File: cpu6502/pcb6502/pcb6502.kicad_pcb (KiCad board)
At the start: 2 copper layers, 134.6 x 95.5 mm, 46 parts, among them J1 Power, J2 RS232, SW1 Reset, SW2 IRQ, SW3 Debug, U1 6502 (CPU), U2 28C256 (ROM), U3 62256 (RAM), U4 6522 (VIA), U5 74HC00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

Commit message: check point again
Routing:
- net /PHI2: track 242.6 -> 239.5 mm, vias 2 -> 1
- net /A11: track 114.5 -> 112.6 mm
- net /CS2: track 143.1 -> 144.2 mm
- net /D2: track 144.2 -> 145.2 mm
- net /R/W: track 188.4 -> 187.6 mm
- net /D1: track 137.6 -> 138.2 mm

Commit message: everything is working well!  OS still wip but pretty good
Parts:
- added J3: VIA PB, Connector_PinHeader_2.54mm:PinHeader_2x05_P2.54mm_Vertical, F.Cu at (76.2, 50.8)
- added J4: Reset Ext, Connector_PinHeader_2.54mm:PinHeader_1x02_P2.54mm_Vertical, F.Cu at (104.1, 29.2)
- C2, C3, C4, C5, C6: footprint Capacitor_THT:C_Disc_D3.0mm_W1.6mm_P2.50mm -> Capacitor_THT:C_Disc_D5.0mm_W2.5mm_P5.00mm
- R5: footprint Resistor_THT:R_Axial_DIN0204_L3.6mm_D1.6mm_P7.62mm_Horizontal -> Resistor_THT:R_Axial_DIN0204_L3.6mm_D1.6mm_P2.54mm_Vertical
- moved R5 8.03 mm to (99.1, 29.2), turned to -90 degrees
- moved SW2 5.09 mm to (76.2, 36.8)
- moved C6 2.58 mm to (191.8, 104.1)
- moved C2 2.50 mm to (191.8, 88.9)
- moved H3 1.42 mm to (74.9, 114.3)
- moved H2 1.27 mm to (74.9, 29.2)
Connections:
- U4 pad 10: unconnected-(U4-PB0-Pad10) -> /PB0
- U4 pad 11: unconnected-(U4-PB1-Pad11) -> /PB1
- U4 pad 12: unconnected-(U4-PB2-Pad12) -> /PB2
- U4 pad 13: unconnected-(U4-PB3-Pad13) -> /PB3
- U4 pad 14: unconnected-(U4-PB4-Pad14) -> /PB4
- U4 pad 15: unconnected-(U4-PB5-Pad15) -> /PB5
- U4 pad 16: unconnected-(U4-PB6-Pad16) -> /PB6
- U4 pad 17: unconnected-(U4-PB7-Pad17) -> /PB7
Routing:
- net +5V: track 500.4 -> 407.6 mm
- net /PB0: track 0.00 -> 87.0 mm
- net /PB1: track 0.00 -> 75.6 mm
- net /PB3: track 0.00 -> 72.6 mm
- net /PB2: track 0.00 -> 71.9 mm
- net /PB5: track 0.00 -> 67.7 mm
- net /PB4: track 0.00 -> 67.1 mm
- net /PB7: track 0.00 -> 62.0 mm
- net /PB6: track 0.00 -> 61.6 mm
- net GND: track 19.6 -> 0.00 mm, vias 1 -> 0
- net /RST: track 291.3 -> 305.4 mm
- net /VIAIRQ: track 58.4 -> 66.1 mm
- net /CA1: track 141.5 -> 148.7 mm, vias 1 -> 0
- net /ACIAIRQ: track 143.9 -> 150.5 mm
- net /R/W: track 187.6 -> 191.3 mm, vias 2 -> 3
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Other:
- board size 134.6 x 95.5 mm -> 135.9 x 95.3 mm
- board text added: "0"
- board text added: "0x0000 - 0x3FFF = RAM (16K) 0x4000 - 0x7FFF = I/O 0x8000 - 0xFFFF = ROM (32K)"
- board text added: "1"
- board text added: "2"
- board text added: "3"
- board text added: "4"
- board text added: "5"
- board text added: "5v"
- board text added: "6"
- board text added: "6502 OAComputer Rev 1.0"
- board text added: "7"
- board text added: "PCB Designed in 2023 by Chris Gall"
- board text added: "Thanks Ben Eater for the inspiration! https://eater.net/6502"
- board text removed: "0x0000 - 0x004F = Reserved OS RAM 0x0050 - 0x00FF = User Zero Page RAM 0x0100 - 0x01FF = Reserved Stack RAM 0x0300 - 0x3FFF = User Program/RAM (~15K) 0x4000 - 0x7FFF = Reserved Hardware 0x8000 - 0xFFFF = ROM (32K)"
- board text removed: "6502 Computer Rev v1.0"

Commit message: check point
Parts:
- removed D10: 4, LED_THT:LED_D3.0mm
- removed D11: 5, LED_THT:LED_D3.0mm
- removed D12: 6, LED_THT:LED_D3.0mm
- removed D13: 7, LED_THT:LED_D3.0mm
- removed D5: 0, LED_THT:LED_D3.0mm
- removed D6: 1, LED_THT:LED_D3.0mm
- removed D8: 2, LED_THT:LED_D3.0mm
- removed D9: 3, LED_THT:LED_D3.0mm
- removed RN2: 220, Resistor_THT:R_Array_SIP8
- C2, C3, C4, C5: value 1uf -> 1µF
- C6: value 20pf -> 20pF
- C7: value 1uF -> 1µF
- C8: value 0.1uf -> 0.1µF
- J3: value VIA PB -> VIA; footprint Connector_PinHeader_2.54mm:PinHeader_2x05_P2.54mm_Vertical -> Connector_PinHeader_2.54mm:PinHeader_2x09_P2.54mm_Vertical
- R3: value 1K -> 1KΩ
- R4: value 1M -> 1MΩ
- R5: value 1K -> 1KΩ; footprint Resistor_THT:R_Axial_DIN0204_L3.6mm_D1.6mm_P2.54mm_Vertical -> Resistor_THT:R_Axial_DIN0204_L3.6mm_D1.6mm_P7.62mm_Horizontal
- RN1: value 220 -> Resistor Array 220Ω (3); footprint Resistor_THT:R_Array_SIP8 -> Resistor_THT:R_Array_SIP6
- SW2: value IRQ -> Interrupts; footprint Button_Switch_THT:SW_DIP_SPSTx03_Slide_9.78x9.8mm_W7.62mm_P2.54mm -> Button_Switch_THT:SW_DIP_SPSTx06_Slide_9.78x17.42mm_W7.62mm_P2.54mm
- moved J3 70.4 mm to (115.6, 109.2), turned to -90 degrees
- moved RN1 30.5 mm to (148.6, 109.2), turned to 180 degrees
- moved R5 5.08 mm to (99.1, 34.3), turned to 90 degrees
- moved SW2 0.26 mm to (76.2, 36.6)
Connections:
- J3 pad 1: /PB0 -> /PA0
- J3 pad 10: GND -> /PB3
- J3 pad 2: /PB1 -> /PB7
- J3 pad 3: /PB2 -> /PA1
- J3 pad 4: /PB3 -> /PB6
- J3 pad 5: /PB4 -> /PA2
- J3 pad 7: /PB6 -> /PA3
- J3 pad 8: /PB7 -> /PB4
- J3 pad 9: +5V -> /PA4
- RN1 pad 2: /RNPA6 -> /RNPA0
- RN1 pad 3: /RNPA5 -> GND
- RN1 pad 4: /RNPA4 -> /RNPA1
- RN1 pad 5: /RNPA3 -> GND
- SW2 pad 4: /VIAIRQ -> /NMI
- SW2 pad 5: /ACIAIRQ -> /NMI
- SW2 pad 6: +5V -> /NMI
- U1 pad 6: +5V -> /NMI
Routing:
- net /NMI: track 0.00 -> 50.0 mm
- net +5V: track 407.6 -> 445.5 mm
- net /PB7: track 62.0 -> 80.1 mm
- net /PB0: track 87.0 -> 69.7 mm
- net /PB6: track 61.6 -> 78.8 mm
- net /PA0: track 59.5 -> 43.6 mm
- net /PA7: track 80.3 -> 69.3 mm
- net /PA1: track 57.4 -> 46.5 mm
- net /RNPA6: track 10.5 -> 0.00 mm
- net /PB5: track 67.7 -> 77.3 mm
- net /RNPA0: track 15.3 -> 6.13 mm
- net /RNPA5: track 8.54 -> 0.00 mm
- net /PA6: track 73.9 -> 65.3 mm
- net /PB4: track 67.1 -> 75.6 mm
- net /RNPA10: track 8.02 -> 0.00 mm
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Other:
- board text added: ". . . . . . ."
- board text added: "ACIA: 5000 - DATA 5001 - STATUS 5002 - COMMAND 5003 - CONTROL"
- board text added: "IRQ"
- board text added: "MEMORY MAP: 0000-3FFF RAM 4000-4FFF N/A 5000-5FFF ACIA 6000-6FFF VIA 7000-7FFF N/A 8000-FFFF ROM"
- board text added: "NMI"
- board text added: "PA0"
- board text added: "PA7"
- board text added: "PB0"
- board text added: "PB7"
- board text added: "VIA: CA1 - DEBUG PB/A - 6000/1 DDRB/A - 6002/3 A/PCR - 600B/C IF/IER - 600D/E"
- board text removed: "0"
- board text removed: "0x0000 - 0x3FFF = RAM (16K) 0x4000 - 0x7FFF = I/O 0x8000 - 0xFFFF = ROM (32K)"
- board text removed: "1"
- board text removed: "2"
- board text removed: "3"
- board text removed: "4"
- board text removed: "5"
- board text removed: "5v"
- board text removed: "6"
- board text removed: "7"
- board text removed: "Gnd"
- board text removed: "RS232, 19200 Baud 8 data bits 1 Stop Bit, No Parity CR only, UPPER case VT100 Emulation"
- board text removed: "User/Status"

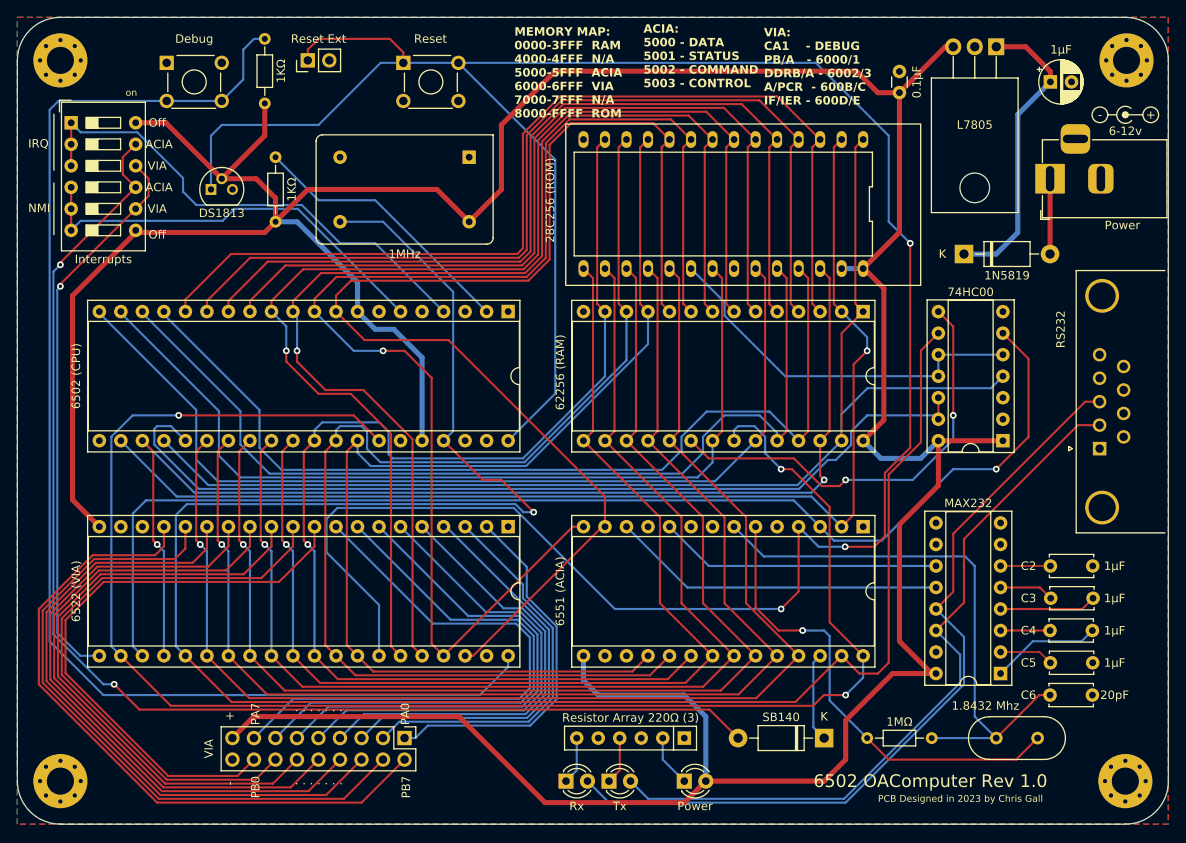
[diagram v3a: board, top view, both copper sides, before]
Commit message: rs232 nmi / cts, circuit close to done
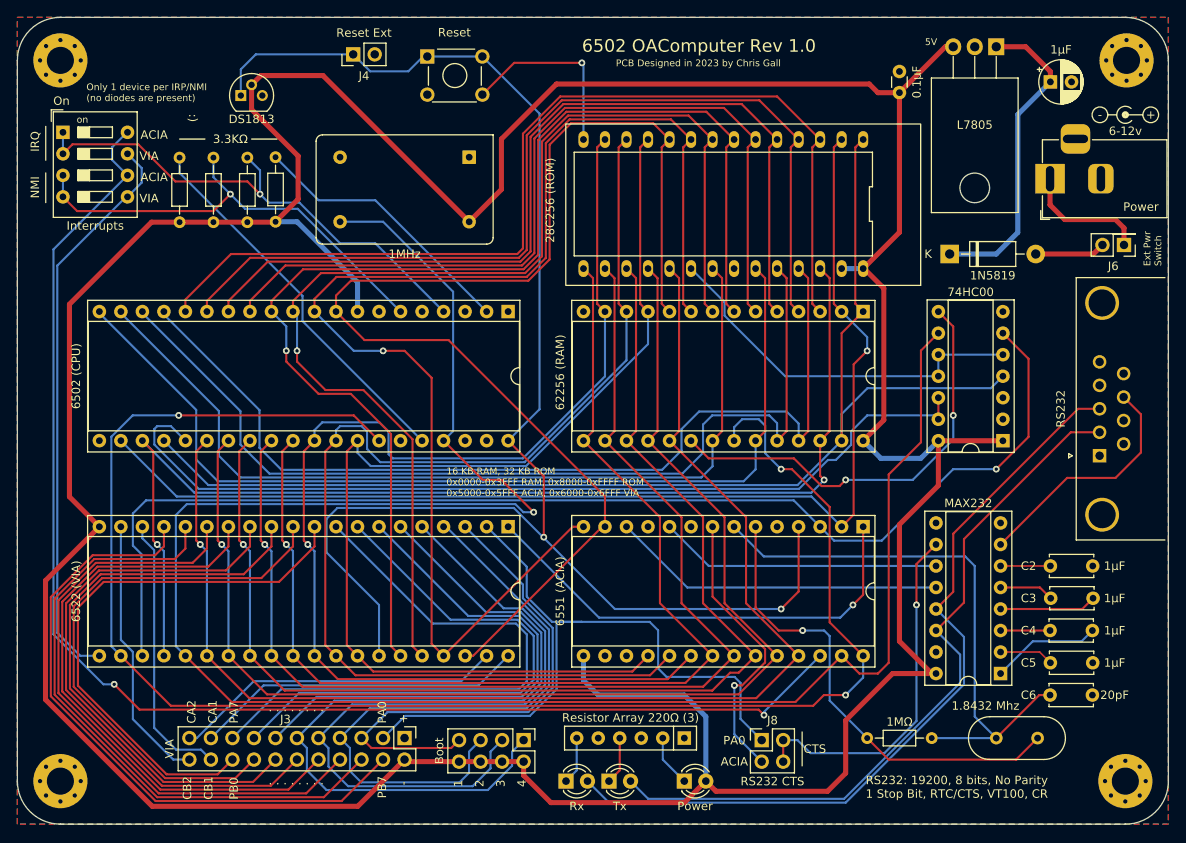
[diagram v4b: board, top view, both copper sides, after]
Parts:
- removed D2: SB140, Diode_THT:D_DO-41_SOD81_P10.16mm_Horizontal
- removed SW3: Debug, Button_Switch_THT:SW_TH_Tactile_Omron_B3F-10xx
- added J5: Boot, Connector_PinHeader_2.54mm:PinHeader_2x04_P2.54mm_Vertical, F.Cu at (129.6, 109.5)
- added J6: Ext Pwr Sw, Connector_PinHeader_2.54mm:PinHeader_2x01_P2.54mm_Vertical, F.Cu at (200.5, 51.0)
- added J8: RS232 CTS, Connector_PinHeader_2.54mm:PinHeader_2x02_P2.54mm_Vertical, F.Cu at (157.7, 109.5)
- added R1: 3.3KΩ, Resistor_THT:R_Axial_DIN0204_L3.6mm_D1.6mm_P7.62mm_Horizontal, F.Cu at (97.0, 48.3)
- added R2: 3.3KΩ, Resistor_THT:R_Axial_DIN0204_L3.6mm_D1.6mm_P7.62mm_Horizontal, F.Cu at (93.0, 48.3)
- J3: footprint Connector_PinHeader_2.54mm:PinHeader_2x09_P2.54mm_Vertical -> Connector_PinHeader_2.54mm:PinHeader_2x11_P2.54mm_Vertical
- R3, R5: value 1KΩ -> 3.3KΩ
- SW2: footprint Button_Switch_THT:SW_DIP_SPSTx06_Slide_9.78x17.42mm_W7.62mm_P2.54mm -> Button_Switch_THT:SW_DIP_SPSTx04_Slide_9.78x12.34mm_W7.62mm_P2.54mm
- moved R5 17.3 mm to (89.0, 48.3)
- moved U9 11.6 mm to (96.2, 33.4)
- moved J4 5.41 mm to (109.5, 28.5)
- moved SW1 2.93 mm to (118.2, 28.8)
- moved D3 1.69 mm to (179.9, 52.1)
- moved SW2 1.48 mm to (75.2, 37.7)
- moved J2 0.84 mm to (197.6, 75.9)
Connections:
- J1 pad 1: Net-(D3-A) -> Net-(J6-Pin_1)
- J2 pad 8: unconnected-(J2-Pad8) -> /RTSINV
- J3 pad 1: /PA0 -> GND
- J3 pad 10: /PB3 -> /PB4
- J3 pad 11: /PA5 -> /PA4
- J3 pad 12: /PB2 -> /PB3
- J3 pad 13: /PA6 -> /PA5
- J3 pad 14: /PB1 -> /PB2
- J3 pad 15: /PA7 -> /PA6
- J3 pad 16: /PB0 -> /PB1
- J3 pad 17: +5V -> /PA7
- J3 pad 18: GND -> /PB0
- J3 pad 2: /PB7 -> +5V
- J3 pad 3: /PA1 -> /PA0
- J3 pad 4: /PB6 -> /PB7
- J3 pad 5: /PA2 -> /PA1
- J3 pad 6: /PB5 -> /PB6
- J3 pad 7: /PA3 -> /PA2
- J3 pad 8: /PB4 -> /PB5
- J3 pad 9: /PA4 -> /PA3
- R5 pad 2: /CA1 -> Net-(U1-BE)
- SW2 pad 3: /IRQ -> /NMI
- SW2 pad 5: /NMI -> /VIAIRQ
- SW2 pad 6: /NMI -> /ACIAIRQ
- SW2 pad 7: +5V -> /VIAIRQ
- SW2 pad 8: /VIAIRQ -> /ACIAIRQ
- U1 pad 36: +5V -> Net-(U1-BE)
- U4 pad 18: unconnected-(U4-CB1-Pad18) -> /CB1
- U4 pad 19: unconnected-(U4-CB2-Pad19) -> /CB2
- U4 pad 39: unconnected-(U4-CA2-Pad39) -> /CA2
- U7 pad 26: Net-(D2-K) -> /ACIAIRQ
- U7 pad 8: unconnected-(U7-~{RTS}-Pad8) -> /ACIARTS
- U8 pad 10: unconnected-(U8-T2IN-Pad10) -> Net-(J8-Pin_2)
- U8 pad 7: unconnected-(U8-T2OUT-Pad7) -> /RTSINV
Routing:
- net /RST: track 309.8 -> 185.2 mm, vias 3 -> 2
- net /CA1: track 153.1 -> 39.1 mm
- net GND: track 0.00 -> 78.1 mm, vias 0 -> 2
- net Net-(U1-BE): track 0.00 -> 45.3 mm
- net Net-(J8-Pin_2): track 0.00 -> 42.3 mm, vias 0 -> 1
- net /PA0: track 43.6 -> 83.9 mm
- net /CA2: track 0.00 -> 39.1 mm
- net /PA4: track 57.4 -> 93.5 mm
- net /ACIARTS: track 0.00 -> 33.7 mm, vias 0 -> 1
- net /CB1: track 0.00 -> 32.6 mm
- net /CB2: track 0.00 -> 32.0 mm
- net /PA3: track 53.5 -> 84.0 mm
- net /RTSINV: track 0.00 -> 28.5 mm
- net /PA2: track 49.5 -> 75.2 mm
- net +5V: track 445.5 -> 469.2 mm
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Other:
- board text added: ". . . . . . . ."
- board text added: "1"
- board text added: "16 KB RAM, 32 KB ROM 0x0000-0x3FFF RAM, 0x8000-0xFFFF ROM 0x5000-0x5FFF ACIA, 0x6000-0x6FFF VIA"
- board text added: "2"
- board text added: "3"
- board text added: "3.3KΩ"
- board text added: "4"
- board text added: "5V"
- board text added: ":)"
- board text added: "CA1"
- board text added: "CA2"
- board text added: "CB1"
- board text added: "CB2"
- board text added: "CTS"
- board text added: "Ext Pwr Switch"
- board text added: "On"
- board text added: "Only 1 device per IRP/NMI (no diodes are present)"
- board text added: "RS232: 19200, 8 bits, No Parity 1 Stop Bit, RTC/CTS, VT100, CR"
- board text removed: ". . . . . . ."
- board text removed: "ACIA: 5000 - DATA 5001 - STATUS 5002 - COMMAND 5003 - CONTROL"
- board text removed: "MEMORY MAP: 0000-3FFF RAM 4000-4FFF N/A 5000-5FFF ACIA 6000-6FFF VIA 7000-7FFF N/A 8000-FFFF ROM"
- board text removed: "Off"
- board text removed: "VIA: CA1 - DEBUG PB/A - 6000/1 DDRB/A - 6002/3 A/PCR - 600B/C IF/IER - 600D/E"

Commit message: more basic progs
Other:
- board text removed: ":)"
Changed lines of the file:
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@@
-		)
-	)
-	(gr_text ":)"
-		(at 90 35.5 270)
-		(layer "F.SilkS")
-		(effects
-			(font
-				(face "Courier New")
-				(size 1 1)
-				(thickness 0.15)
-			)
-			(justify left bottom)
-		)
-		(render_cache ":)" 270
-			(polygon
-				(pts
-					(xy 90.763998 35.910083) (xy 90.763998 35.934996) (xy 90.750953 35.982527) (xy 90.736399 36.000697)
-					(xy 90.693601 36.025602) (xy 90.670942 36.028297) (xy 90.623402 36.016306) (xy 90.603286 36.000453)
-					(xy 90.579043 35.95755) (xy 90.57642 35.934996) (xy 90.57642 35.910083) (xy 90.589465 35.862437)
-					(xy 90.604019 35.844138) (xy 90.646817 35.819454) (xy 90.669476 35.816782) (xy 90.717015 35.828774)
-					(xy 90.737131 35.844626) (xy 90.761374 35.887529)
-				)
-			)
-			(polygon
-				(pts
-					(xy 90.341946 35.910083) (xy 90.341946 35.934996) (xy 90.329017 35.982527) (xy 90.314591 36.000697)
-					(xy 90.271552 36.025602) (xy 90.248401 36.028297) (xy 90.199443 36.015136) (xy 90.181235 36.000453)
-					(xy 90.156992 35.95755) (xy 90.154368 35.934996) (xy 90.154368 35.910083) (xy 90.167298 35.862437)
-					(xy 90.181723 35.844138) (xy 90.224762 35.819454) (xy 90.247913 35.816782) (xy 90.296756 35.829943)
-					(xy 90.314836 35.844626) (xy 90.339299 35.887529)
-				)
-			)
-			(polygon
-				(pts
-					(xy 90.513649 36.779099) (xy 90.463742 36.777072) (xy 90.412021 36.77099) (xy 90.363923 36.762049)
-					(xy 90.347564 36.758339) (xy 90.296177 36.743804) (xy 90.246802 36.725856) (xy 90.200744 36.706269)
-					(xy 90.15202 36.68306) (xy 90.144842 36.679448) (xy 90.098717 36.655429) (xy 90.052397 36.629012)
-					(xy 90.011275 36.599722) (xy 90.006113 36.594452) (xy 89.998053 36.576622) (xy 90.006601 36.555617)
-					(xy 90.026629 36.547069) (xy 90.041528 36.551953) (xy 90.092017 36.578735) (xy 90.140721 36.602477)
-					(xy 90.187638 36.62318) (xy 90.240118 36.643491) (xy 90.290167 36.659665) (xy 90.339012 36.672227)
-					(xy 90.38788 36.681704) (xy 90.436772 36.688095) (xy 90.485687 36.691401) (xy 90.513649 36.691905)
-					(xy 90.562768 36.690362) (xy 90.611817 36.685734) (xy 90.660795 36.67802) (xy 90.709704 36.667221)
-					(xy 90.73762 36.659665) (xy 90.787704 36.643491) (xy 90.840289 36.62318) (xy 90.887352 36.602477)
-					(xy 90.936253 36.578735) (xy 90.986992 36.551953) (xy 91.001891 36.547069) (xy 91.02143 36.555617)
-					(xy 91.029734 36.576622) (xy 91.022163 36.594452) (xy 90.980943 36.625349) (xy 90.937304 36.650689)
-					(xy 90.893558 36.673923) (xy 90.886608 36.677494) (xy 90.838693 36.701006) (xy 90.793256 36.721105)
-					(xy 90.744361 36.739896) (xy 90.693223 36.755709) (xy 90.687794 36.757117) (xy 90.639063 36.767743)
-					(xy 90.590138 36.774892) (xy 90.54102 36.778563)
-				)
-			)
 		)
 	)

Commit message: pcb updates
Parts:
- removed RN1: Resistor Array 220Ω (3), Resistor_THT:R_Array_SIP6
- removed SW2: Interrupts, Button_Switch_THT:SW_DIP_SPSTx04_Slide_9.78x12.34mm_W7.62mm_P2.54mm
- added J7: Interrupts, Connector_PinHeader_2.54mm:PinHeader_2x04_P2.54mm_Vertical, F.Cu at (75.5, 37.9)
- added R6: 220Ω, Resistor_THT:R_Axial_DIN0204_L3.6mm_D1.6mm_P2.54mm_Vertical, F.Cu at (134.5, 110.0)
- added R7: 220Ω, Resistor_THT:R_Axial_DIN0204_L3.6mm_D1.6mm_P2.54mm_Vertical, F.Cu at (140.0, 110.2)
- added R8: 220Ω, Resistor_THT:R_Axial_DIN0204_L3.6mm_D1.6mm_P2.54mm_Vertical, F.Cu at (147.3, 110.5)
- moved J5 0.23 mm to (129.6, 109.2)
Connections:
- U7 pad 11: unconnected-(U7-~{DTR}-Pad11) -> GND
- U7 pad 16: unconnected-(U7-~{DCD}-Pad16) -> GND
- U7 pad 17: unconnected-(U7-~{DSR}-Pad17) -> GND
- U7 pad 9: unconnected-(U7-~{CTS}-Pad9) -> GND
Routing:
- net GND: track 78.1 -> 56.5 mm, vias 2 -> 1
- net /RxD: track 39.5 -> 43.5 mm, vias 0 -> 1
- net /PA0: track 83.9 -> 80.6 mm, vias 0 -> 2
- net /ACIAIRQ: track 162.0 -> 159.3 mm
- net /VIAIRQ: track 68.2 -> 65.5 mm
- net /TxD: track 33.4 -> 35.8 mm, vias 0 -> 1
- net /RNPA0: track 6.13 -> 4.34 mm
- net /RNPA1: track 5.61 -> 4.20 mm
- net /RNPA2: track 5.61 -> 4.35 mm
